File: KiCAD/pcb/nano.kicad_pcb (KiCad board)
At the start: 2 copper layers, 69.8 x 49.5 mm, 24 parts, among them J1 Barrel_Jack_Switch, J2 Conn_01x02_Male, J3 Conn_01x02_Male, J4 Conn_01x04_Male, J5 Conn_01x03_Male, K1 SANYOU_SRD_Form_C, K2 SANYOU_SRD_Form_C, P1 Digital, P2 Analog, Q1 S8050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

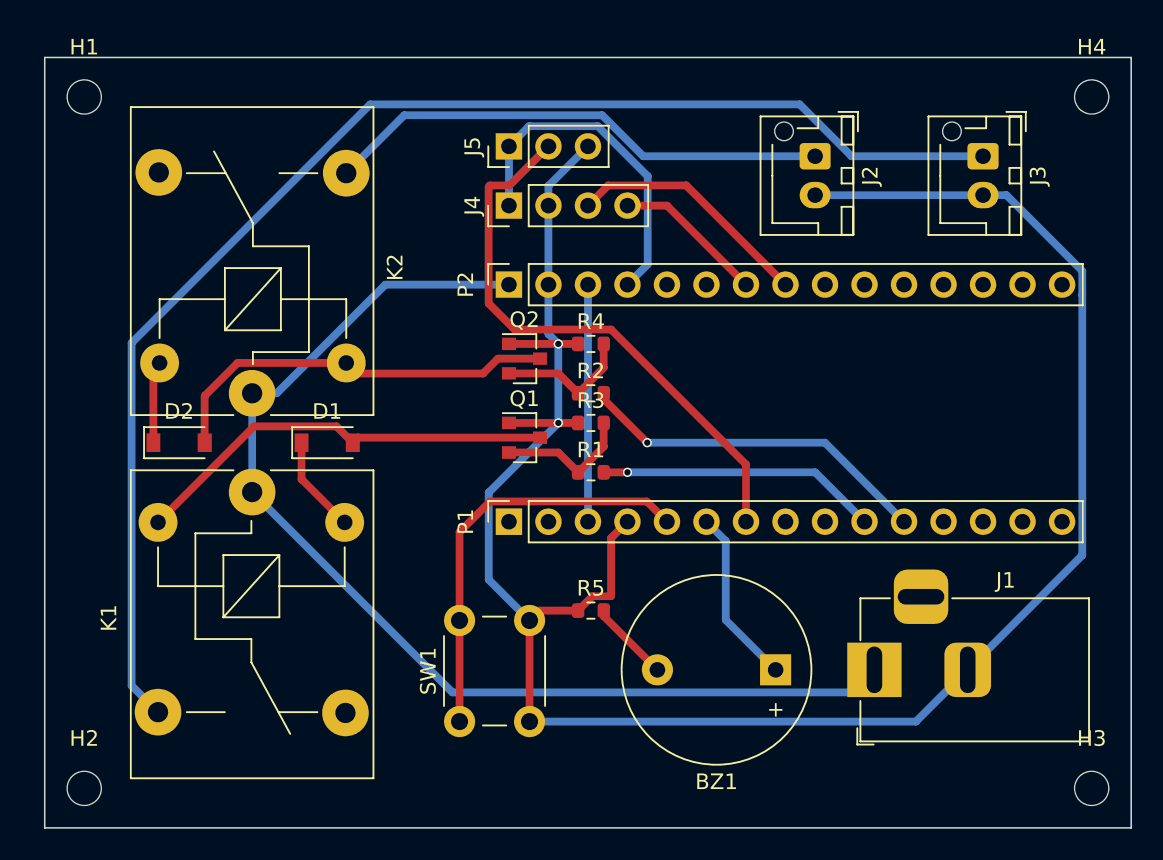
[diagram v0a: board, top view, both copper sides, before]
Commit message: upgrade to KiCAD 6
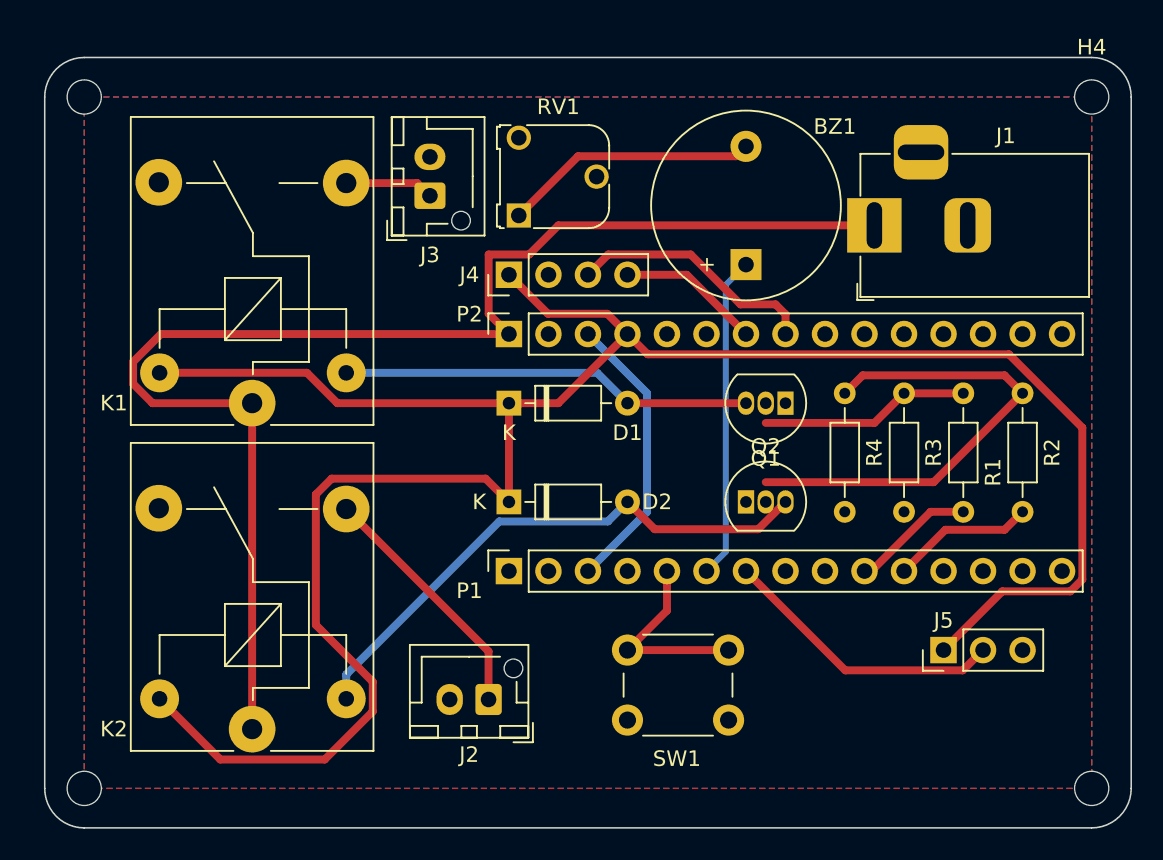
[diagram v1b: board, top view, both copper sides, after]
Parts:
- removed R5: R, Resistor_SMD:R_0603_1608Metric
- added RV1: 10K, Potentiometer_THT:Potentiometer_Runtron_RM-065_Vertical, F.Cu at (151.1, 102.2)
- D1, D2: footprint Diode_SMD:D_SOD-123 -> Diode_THT:D_DO-35_SOD27_P7.62mm_Horizontal
- Q1, Q2: footprint Package_TO_SOT_SMD:SOT-23 -> Package_TO_SOT_THT:TO-92_Inline
- R1, R2: value R -> 1K; footprint Resistor_SMD:R_0603_1608Metric -> Resistor_THT:R_Axial_DIN0204_L3.6mm_D1.6mm_P7.62mm_Horizontal
- R3, R4: value R -> 10K; footprint Resistor_SMD:R_0603_1608Metric -> Resistor_THT:R_Axial_DIN0204_L3.6mm_D1.6mm_P7.62mm_Horizontal
- moved J5 42.8 mm to (178.4, 130.2)
- moved J2 40.7 mm to (149.2, 133.3), turned to 180 degrees
- moved J3 35.7 mm to (145.4, 101.0), turned to 90 degrees
- moved J1 28.6 mm to (174.0, 102.9)
- moved R2 27.8 mm to (183.5, 113.7), turned to -90 degrees
- moved BZ1 26.1 mm to (165.7, 105.4), turned to 90 degrees
- moved R1 24.5 mm to (179.7, 113.7), turned to -90 degrees
- moved K2 21.6 mm to (134.0, 135.3)
- moved D2 21.5 mm to (150.5, 120.7)
- moved R3 20.9 mm to (175.9, 121.3), turned to 90 degrees
- moved R4 19.6 mm to (172.1, 121.3), turned to 90 degrees
- moved Q2 17.0 mm to (165.7, 120.7)
- moved Q1 16.9 mm to (168.3, 114.3), turned to 180 degrees
- moved D1 12.0 mm to (150.5, 114.3)
- moved SW1 11.7 mm to (158.1, 130.2), turned to 0 degrees
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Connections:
- D1 pad 1: Net-(D1-Pad1) -> +5V
- D2 pad 1: Net-(D2-Pad1) -> +5V
- J1 pad 3: (no net) -> unconnected-(J1-Pad3)
- K1 pad 4: (no net) -> unconnected-(K1-Pad4)
- K1 pad 5: Net-(D1-Pad1) -> +5V
- K2 pad 4: (no net) -> unconnected-(K2-Pad4)
- K2 pad 5: Net-(D2-Pad1) -> +5V
- P1 pad 1: (no net) -> /1(Tx)
- P1 pad 12: (no net) -> /9(**)
- P1 pad 13: (no net) -> /10(SS)
- P1 pad 14: (no net) -> /11(MOSI)
- P1 pad 15: (no net) -> /12(MISO)
- P1 pad 2: (no net) -> /0(Rx)
- P1 pad 8: (no net) -> /5(**)
- P1 pad 9: (no net) -> /6(**)
- P2 pad 10: (no net) -> /A2
- P2 pad 11: (no net) -> /A1
- P2 pad 12: (no net) -> /A0
- P2 pad 13: (no net) -> /AREF
- P2 pad 14: (no net) -> unconnected-(P2-Pad14)
- P2 pad 15: (no net) -> /13(SCK)
- P2 pad 5: (no net) -> /A7
- P2 pad 6: (no net) -> /A6
- P2 pad 9: (no net) -> /A3
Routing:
- net GND: track 138.7 -> 0.00 mm, vias 2 -> 0
- net +5V: track 22.1 -> 146.1 mm
- net HEATER_VCC: track 86.9 -> 5.72 mm
- net Net-(Q2-Pad2): track 8.83 -> 31.3 mm
- net DHT11: track 36.9 -> 18.4 mm
- net FAN_VCC: track 32.8 -> 16.0 mm
- net +12V: track 71.7 -> 86.7 mm
- net CTRL: track 26.9 -> 12.6 mm
- net FAN_RELAY: track 22.9 -> 9.20 mm, vias 1 -> 0
- net Net-(BZ1-Pad2): track 5.24 -> 16.4 mm
- net HEATER_RELAY: track 18.1 -> 7.93 mm, vias 1 -> 0
- net Net-(D2-Pad2): track 26.1 -> 35.8 mm
- net BUZZER: track 11.4 -> 20.8 mm
- net Net-(D1-Pad1): track 6.27 -> 0.00 mm
- net Net-(D2-Pad1): track 5.29 -> 0.00 mm
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- added copper zone on B.Cu, net GND
- added copper zone on F.Cu, net GND
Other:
- outline, holes or cut-outs redrawn
- net class Default removed

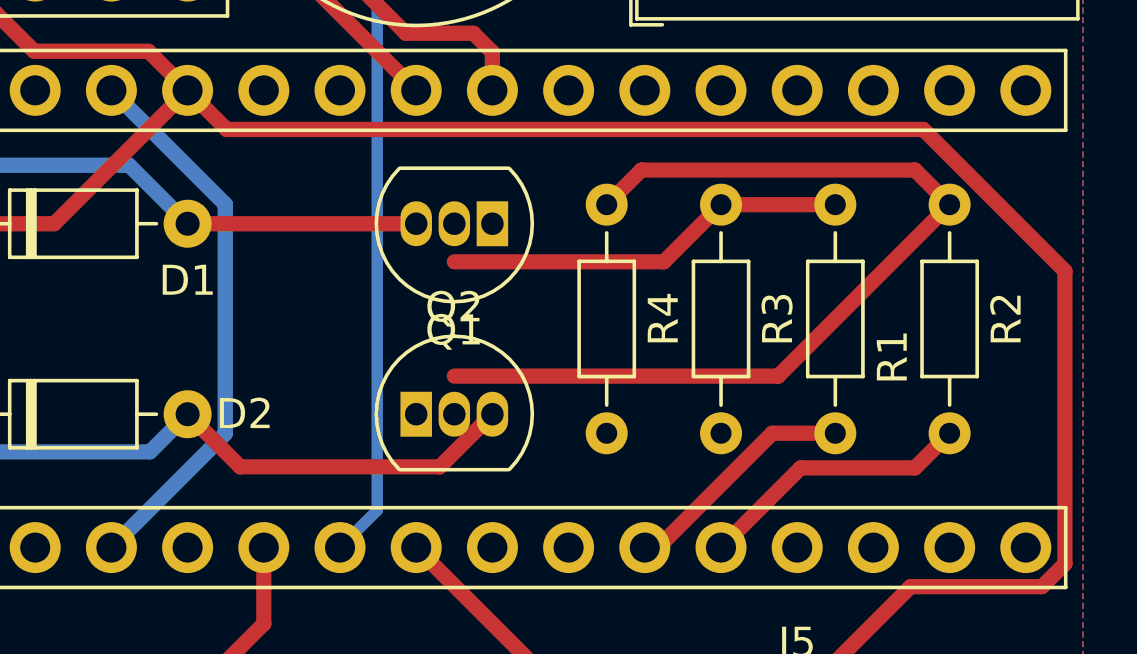
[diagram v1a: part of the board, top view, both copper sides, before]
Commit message: fixed unlinked pads
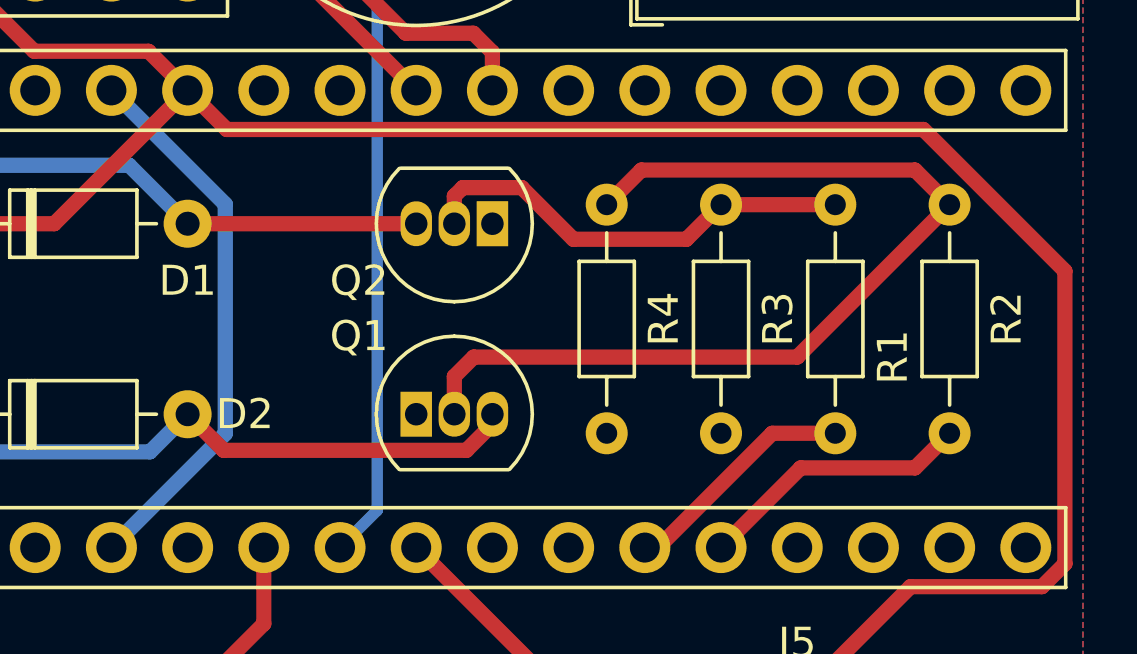
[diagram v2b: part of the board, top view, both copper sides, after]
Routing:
- net Net-(Q1-Pad2): track 13.5 -> 14.9 mm
- net Net-(Q2-Pad2): track 31.3 -> 32.5 mm
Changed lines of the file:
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@@
     (property "Sheetname" "")
     (attr through_hole)
-    (fp_text reference "Q1" (at 1.27 -3.56 180) (layer "F.SilkS")
+    (fp_text reference "Q1" (at 4.445 -3.75 180) (layer "F.SilkS")
       (effects (font (size 1 1) (thickness 0.15)))
     )
@@
     (property "Sheetname" "")
     (attr through_hole)
-    (fp_text reference "Q2" (at 1.27 -3.56) (layer "F.SilkS")
+    (fp_text reference "Q2" (at -1.905 -4.445) (layer "F.SilkS")
       (effects (font (size 1 1) (thickness 0.15)))
     )
@@
   (segment (start 158.115 114.3) (end 156.165 112.35) (width 0.508) (layer "B.Cu") (net 6))
   (segment (start 156.165 112.35) (end 140.035 112.35) (width 0.508) (layer "B.Cu") (net 6))
-  (segment (start 158.115 120.65) (end 159.869001 122.404001) (width 0.508) (layer "F.Cu") (net 8))
-  (segment (start 159.869001 122.404001) (end 166.520999 122.404001) (width 0.508) (layer "F.Cu") (net 8))
-  (segment (start 166.520999 122.404001) (end 168.275 120.65) (width 0.508) (layer "F.Cu") (net 8))
+  (segment (start 168.275 120.988836) (end 168.275 120.65) (width 0.508) (layer "F.Cu") (net 8))
+  (segment (start 158.115 120.65) (end 159.318511 121.853511) (width 0.508) (layer "F.Cu") (net 8))
+  (segment (start 159.318511 121.853511) (end 167.410325 121.853511) (width 0.508) (layer "F.Cu") (net 8))
+  (segment (start 167.410325 121.853511) (end 168.275 120.988836) (width 0.508) (layer "F.Cu") (net 8))
   (segment (start 149.876489 121.903511) (end 140.035 131.745) (width 0.508) (layer "B.Cu") (net 8))
   (segment (start 156.861489 121.903511) (end 149.876489 121.903511) (width 0.508) (layer "B.Cu") (net 8))
@@
   (segment (start 160.655 127.635) (end 158.115 130.175) (width 0.508) (layer "F.Cu") (net 18))
   (segment (start 164.615 130.175) (end 158.115 130.175) (width 0.508) (layer "F.Cu") (net 18))
-  (segment (start 173.99 115.57) (end 167.005 115.57) (width 0.508) (layer "F.Cu") (net 19))
   (segment (start 179.705 113.665) (end 175.895 113.665) (width 0.508) (layer "F.Cu") (net 19))
-  (segment (start 175.895 113.665) (end 173.99 115.57) (width 0.508) (layer "F.Cu") (net 19))
+  (segment (start 169.253511 113.096489) (end 167.286715 113.096489) (width 0.508) (layer "F.Cu") (net 19))
+  (segment (start 170.975533 114.818511) (end 169.253511 113.096489) (width 0.508) (layer "F.Cu") (net 19))
+  (segment (start 167.005 113.378204) (end 167.005 114.3) (width 0.508) (layer "F.Cu") (net 19))
+  (segment (start 175.895 113.665) (end 174.741489 114.818511) (width 0.508) (layer "F.Cu") (net 19))
+  (segment (start 167.286715 113.096489) (end 167.005 113.378204) (width 0.508) (layer "F.Cu") (net 19))
+  (segment (start 174.741489 114.818511) (end 170.975533 114.818511) (width 0.508) (layer "F.Cu") (net 19))
   (segment (start 182.360999 112.510999) (end 173.239001 112.510999) (width 0.508) (layer "F.Cu") (net 20))
-  (segment (start 167.005 119.38) (end 177.8 119.38) (width 0.508) (layer "F.Cu") (net 20))
+  (segment (start 167.652 118.745) (end 167.005 119.392) (width 0.508) (layer "F.Cu") (net 20))
   (segment (start 183.515 113.665) (end 182.360999 112.510999) (width 0.508) (layer "F.Cu") (net 20))
+  (segment (start 178.435 118.745) (end 167.652 118.745) (width 0.508) (layer "F.Cu") (net 20))
   (segment (start 173.239001 112.510999) (end 172.085 113.665) (width 0.508) (layer "F.Cu") (net 20))
-  (segment (start 177.8 119.38) (end 183.515 113.665) (width 0.508) (layer "F.Cu") (net 20))
+  (segment (start 167.005 119.392) (end 167.005 120.65) (width 0.508) (layer "F.Cu") (net 20))
+  (segment (start 183.515 113.665) (end 178.435 118.745) (width 0.508) (layer "F.Cu") (net 20))
   (zone (net 2) (net_name "GND") (layer "F.Cu") (hatch edge 0.508)
     (connect_pads (clearance 0.508))

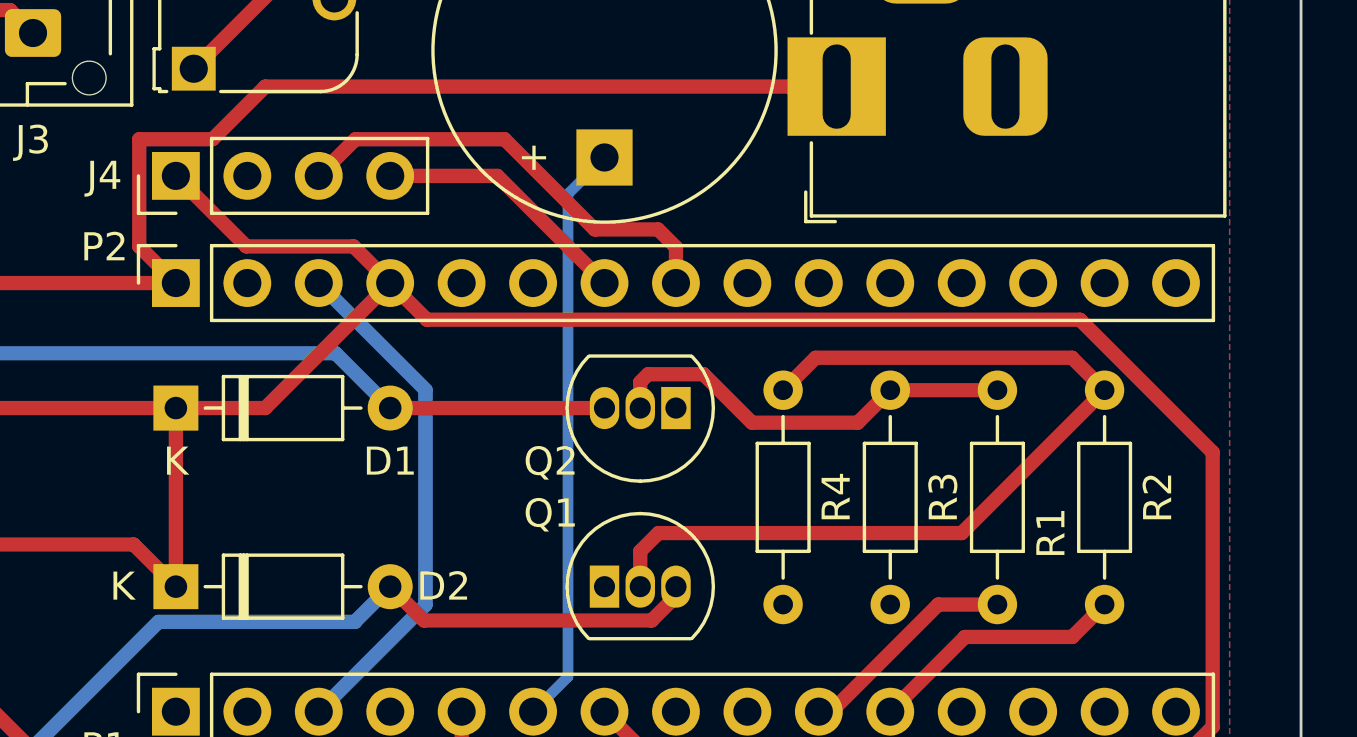
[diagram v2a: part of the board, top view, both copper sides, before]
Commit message: fixed LCD cable sequence
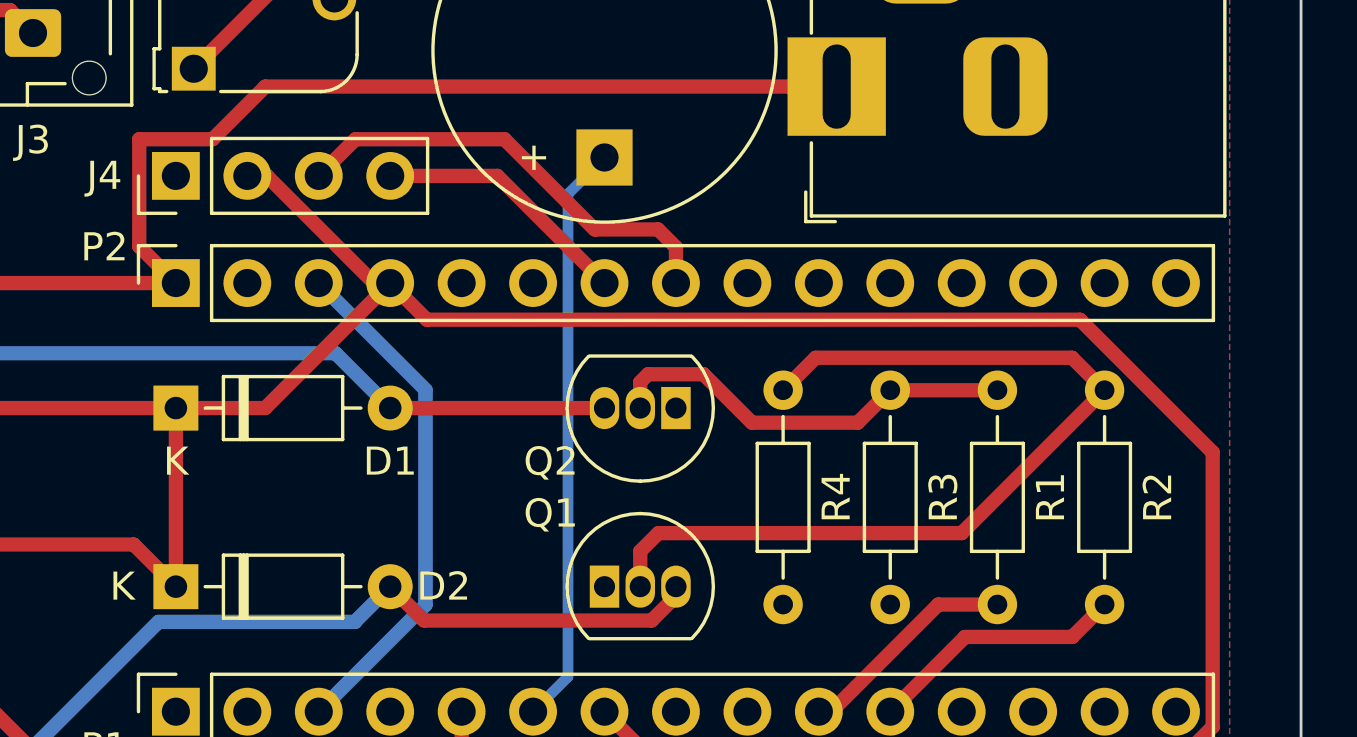
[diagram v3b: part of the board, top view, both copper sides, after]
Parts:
- moved R1 7.62 mm to (179.7, 121.3), turned to 90 degrees
- moved R2 7.62 mm to (183.5, 121.3), turned to 90 degrees
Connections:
- J4 pad 1: +5V -> GND
- J4 pad 2: GND -> +5V
- R1 pad 1: Net-(Q1-Pad2) -> HEATER_RELAY
- R1 pad 2: HEATER_RELAY -> Net-(Q1-Pad2)
- R2 pad 1: Net-(Q2-Pad2) -> FAN_RELAY
- R2 pad 2: FAN_RELAY -> Net-(Q2-Pad2)
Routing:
- net +5V: track 146.1 -> 143.6 mm

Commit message: PCB rearranged
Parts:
- moved J1 43.6 mm to (130.8, 108.6), turned to -90 degrees
- moved Q2 37.8 mm to (128.3, 115.6), turned to 90 degrees
- moved Q1 34.9 mm to (133.3, 113.0), turned to -90 degrees
- moved J5 33.7 mm to (181.0, 96.5), turned to -90 degrees
- moved J2 30.5 mm to (140.3, 104.1), turned to 90 degrees
- moved RV1 27.4 mm to (164.1, 126.3)
- moved J4 22.4 mm to (170.8, 96.5), turned to -90 degrees
- moved BZ1 20.2 mm to (174.0, 123.8), turned to 0 degrees
- moved D2 18.2 mm to (158.1, 104.1), turned to -90 degrees
- moved K1 17.4 mm to (150.5, 119.8), turned to -90 degrees
- moved D1 15.8 mm to (162.6, 104.1), turned to -90 degrees
- moved J3 14.3 mm to (140.3, 114.3)
- moved R4 10.3 mm to (168.3, 111.8)
- moved P2 9.87 mm to (148.0, 100.3)
- moved P1 9.86 mm to (148.0, 115.6)
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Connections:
- P1 pad 3: /Reset -> /Reset1
- P2 pad 3: /Reset -> /Reset2
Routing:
- net Net-(Q1-Pad2): track 14.9 -> 57.4 mm
- net Net-(D2-Pad2): track 35.6 -> 68.6 mm
- net DHT11: track 18.4 -> 46.6 mm
- net Net-(Q2-Pad2): track 32.5 -> 60.4 mm
- net Net-(D1-Pad2): track 26.5 -> 45.5 mm
- net /Reset: track 18.4 -> 0.00 mm
- net HEATER_VCC: track 5.72 -> 23.9 mm
- net ICD_I2C_SDA: track 16.1 -> 3.80 mm
- net CTRL: track 12.6 -> 24.1 mm
- net +5V: track 143.6 -> 133.8 mm
- net LCD_I2C_SCL: track 9.20 -> 3.80 mm
- net BUZZER: track 20.8 -> 16.8 mm
- net FAN_VCC: track 16.0 -> 19.6 mm
- net FAN_RELAY: track 9.20 -> 11.7 mm
- net Net-(BZ1-Pad2): track 16.4 -> 18.5 mm
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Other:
- board text added: "Nano Proofing Box ITEA Trade Ltd. (C)2021-2022"
